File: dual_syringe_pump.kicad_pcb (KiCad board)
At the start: 2 copper layers, 100.3 x 85.5 mm, 163 parts, among them J2 Barrel_Jack_Switch_Pin3Ring, Q1 SS8050, Q2 SS8050, Q3 SS8050, Q4 SS8050, U1 ESP32-WROOM-32, U2 AMS1117-3.3, U3 CH340C, U4 TP5100, U5 LM2596S-buck, U6 TMC2209-LA, U7 TMC2209-LA

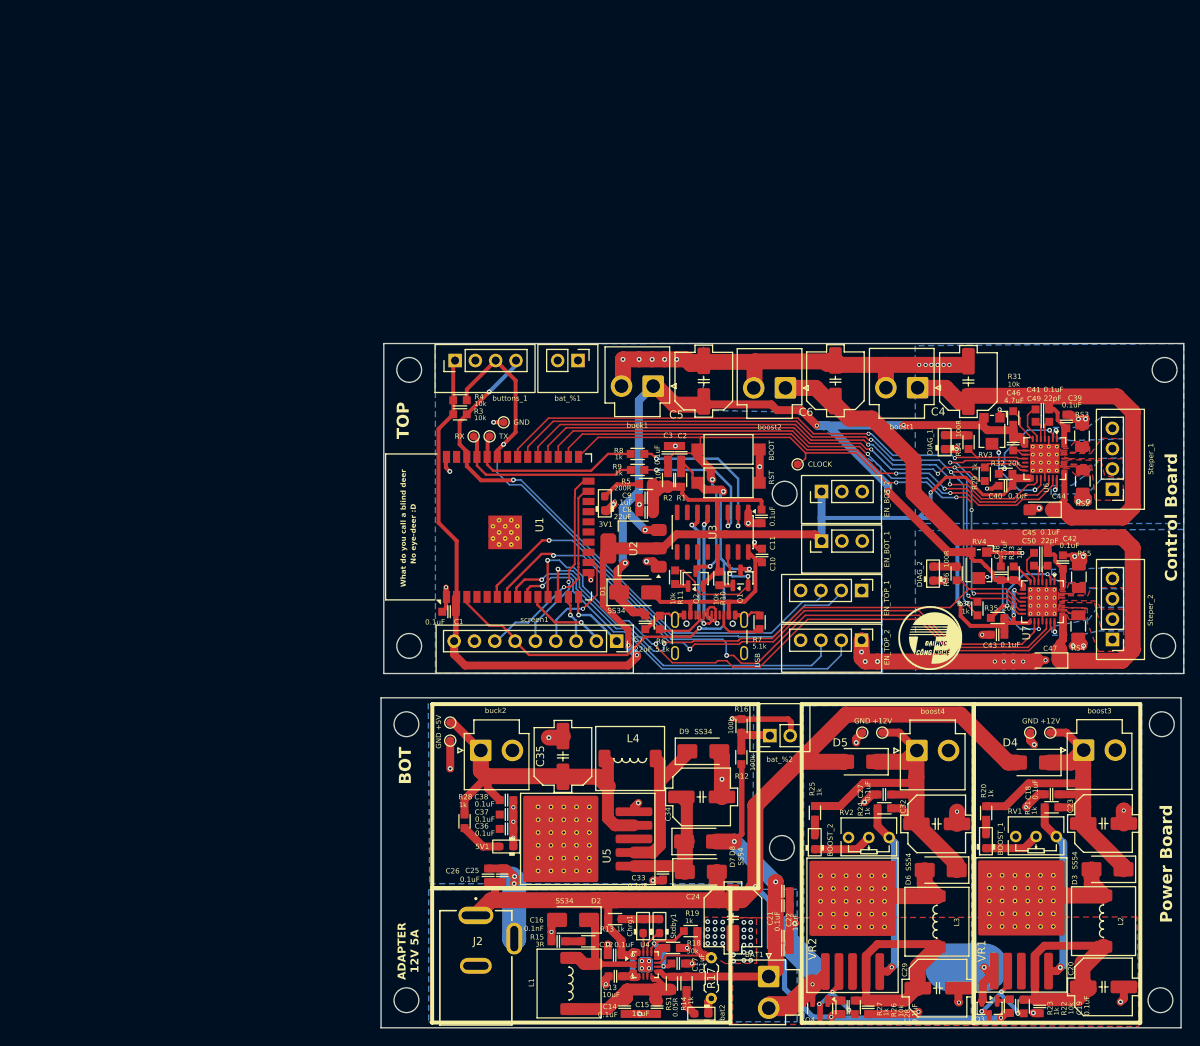
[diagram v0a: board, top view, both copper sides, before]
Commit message: added power button
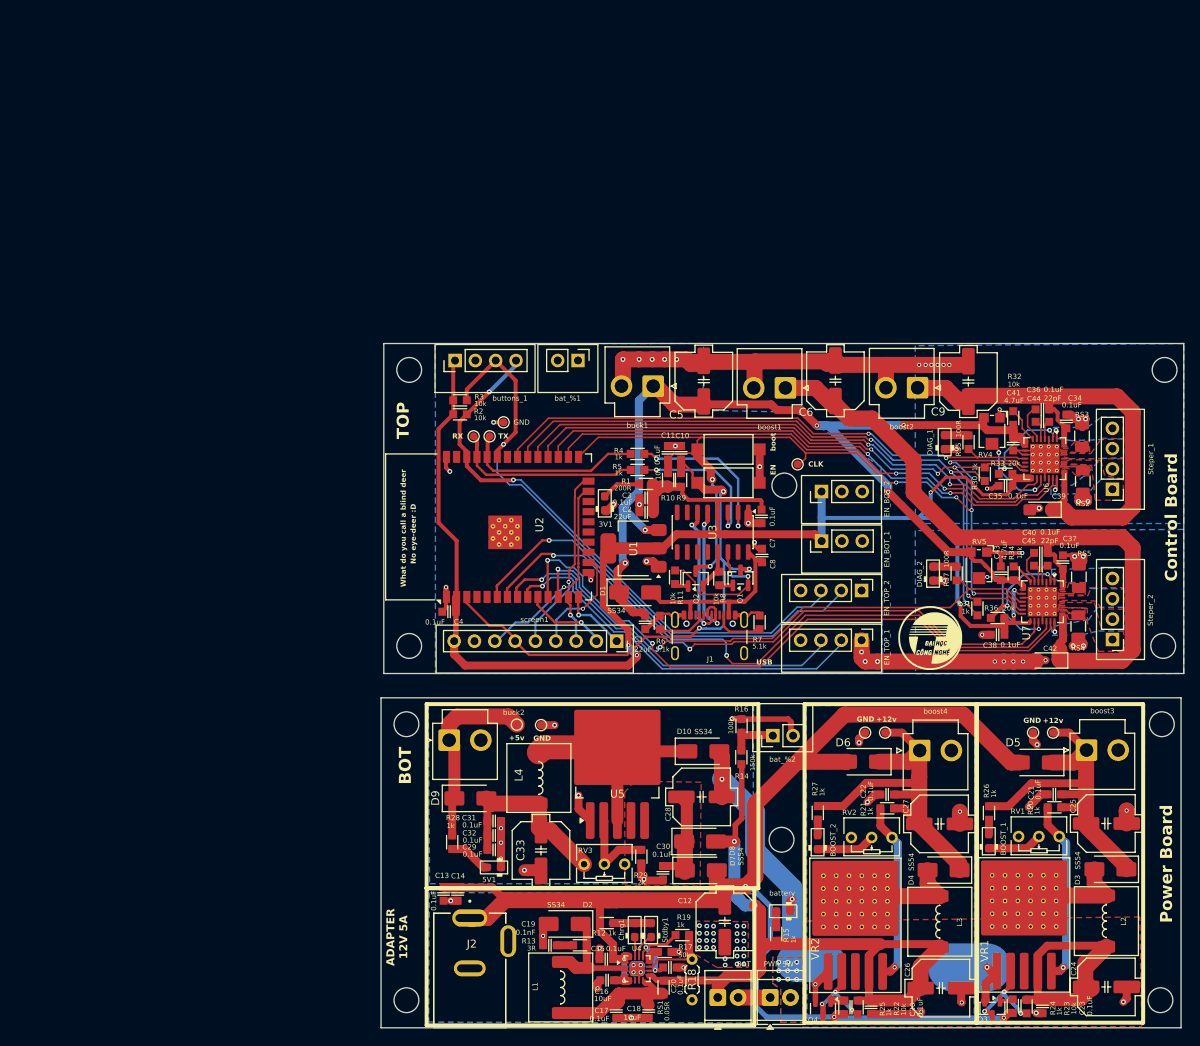
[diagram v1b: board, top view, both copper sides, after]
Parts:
- removed the C21 at (109.8, 93.1)
- removed the C22 at (109.8, 94.8)
- removed the C30 at (109.8, 87.5)
- removed the C31 at (109.8, 89.3)
- added D9: SS34, Diode_SMD:D_SMA, F.Cu at (70.8, 75.9)
- added PWR SW: pb, TerminalBlock_TE-Connectivity:TerminalBlock_TE_282834-2_1x02_P2.54mm_Horizontal, F.Cu at (108.2, 100.8)
- added R29: 2k, PCM_4ms_Resistor:R_0603, F.Cu at (92.1, 83.2)
- added RV3: 10k, PCM_Potentiometer_THT_AKL_Double:Potentiometer_Bourns_3266Y_Vertical, F.Cu at (85.0, 84.1)
- BAT: renamed from BAT1; footprint Connector_JST:JST_VH_B2P-VH-B_1x02_P3.96mm_Vertical -> TerminalBlock_TE-Connectivity:TerminalBlock_TE_282834-2_1x02_P2.54mm_Horizontal
- R14: renamed from R12; value 100k -> 150k
- TP1: renamed from CLOCK; value TestPoint -> clock
- TP2: renamed from RX; value TestPoint -> rx
- TP3: renamed from TX; value TestPoint -> tx
- U5: value LM2596S-buck -> XL4015; footprint PCM_Package_TO_SOT_SMD_AKL:TO-263-5_TabPin3_ThermalVias -> Package_TO_SOT_SMD:TO-263-5_TabPin3
- moved battery 16.4 mm to (109.9, 90.0)
- moved R15 12.8 mm to (109.0, 92.8), turned to -90 degrees
- moved C33 12.1 mm to (79.6, 82.4), turned to -90 degrees
- moved L4 11.7 mm to (79.3, 73.3), turned to -90 degrees
- moved TP7 11.5 mm to (79.6, 66.7), turned to 180 degrees
- moved U5 10.6 mm to (89.1, 71.0), turned to 90 degrees
- moved TP8 8.33 mm to (76.6, 66.7), turned to 180 degrees
- moved C14 7.68 mm to (67.4, 87.8), turned to -90 degrees
- moved BAT 6.88 mm to (101.7, 100.8), turned to 0 degrees
- moved C13 4.48 mm to (69.2, 87.8), turned to -90 degrees
- moved buck2 4.15 mm to (68.1, 68.6)
- moved 5V1 3.04 mm to (73.7, 84.5)
- moved C29 3.04 mm to (73.8, 82.3)
- moved C31 3.04 mm to (73.8, 78.7)
- moved C32 3.04 mm to (73.8, 80.5)
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- renumbered C7 to C1, C2 to C10, C3 to C11, C24 to C12, C25 to C13, C26 to C14, C12 to C15, C13 to C16, C14 to C17, C15 to C18, C16 to C19, C8 to C2, C17 to C20, C18 to C21, C27 to C22, C19 to C23, C20 to C24, C23 to C25, C29 to C26, C32 to C27, C34 to C28, C36 to C29, C9 to C3, C33 to C30, C28 to C30, C38 to C31, C37 to C32, C35 to C33, C39 to C34, C40 to C35, C41 to C36, C42 to C37, C43 to C38, C44 to C39, C1 to C4, C45 to C40, C46 to C41, C47 to C42, C48 to C43, C49 to C44, C50 to C45, C11 to C7, C10 to C8, C4 to C9, D9 to D10, D6 to D4, D4 to D5, D5 to D6, EN_TOP_2 to EN_TOP_1, EN_TOP_1 to EN_TOP_2, USB to J1, R5 to R1, R2 to R10, R13 to R12, R15 to R13, R14 to R15, R18 to R17, R17 to R18, R3 to R2, R21 to R20, R24 to R21, R26 to R22, R22 to R23, R23 to R24, R27 to R25, R20 to R26, R25 to R27, R4 to R3, R29 to R30, R30 to R31, R31 to R32, R32 to R33, R33 to R34, R34 to R35, R35 to R36, R36 to R37, R8 to R4, R9 to R5, R10 to R8, R1 to R9, RV3 to RV4, RV4 to RV5, RST to SW1, BOOT to SW2, +12V to TP4, +12V to TP5, GND to TP6, GND to TP7, +5V to TP8, GND to TP9, U2 to U1, U1 to U2, bat2 to battery, boost2 to boost1, boost1 to boost2
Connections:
- net /BTN1 renamed /bat%
- BAT pad 2: GND -> Earth
- C12 pad 2: GND -> Earth
- C13 pad 2: GND -> Earth
- C14 pad 2: GND -> Earth
- C15 pad 2: GND -> Earth
- C16 pad 2: GND -> Earth
- C17 pad 2: GND -> Earth
- C18 pad 2: GND -> Earth
- C19 pad 2: GND -> Earth
- C20 pad 2: GND -> Earth
- C29 pad 1: +5V -> Net-(D9-A)
- C31 pad 1: +5V -> Net-(D9-A)
- C32 pad 1: +5V -> Net-(D9-A)
- C33 pad 1: +5V -> Net-(D9-A)
- D10 pad 1: Net-(D9-K) -> Net-(D10-K)
- D2 pad 2: GND -> Earth
- J2 pad 2: GND -> Earth
- J2 pad 3: GND -> Earth
- L4 pad 1: Net-(D9-K) -> Net-(D10-K)
- L4 pad 2: +5V -> Net-(D9-A)
- R17 pad 1: GND -> Earth
- R18 pad 1: GND -> Earth
- R22 pad 1: Net-(Q4-C) -> Vbat
- R22 pad 2: Vbat -> Net-(Q4-C)
- R23 pad 1: Net-(Q3-C) -> Vbat
- R23 pad 2: Vbat -> Net-(Q3-C)
- U2 pad 4: /BTN2 -> unconnected-(U2-SENSOR_VP-Pad4)
- U2 pad 5: /BTN3 -> unconnected-(U2-SENSOR_VN-Pad5)
- U4 pad 17: GND -> Earth
- U4 pad 7: GND -> Earth
- U5 pad 1: Net-(D7-K) -> GND
- U5 pad 2: Net-(D9-K) -> /Power Circuits/FB
- U5 pad 3: GND -> Net-(D10-K)
- U5 pad 4: +5V -> Net-(D7-K)
- U5 pad 5: GND -> Net-(D7-K)
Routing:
- net Net-(D10-K): track 0.00 -> 28.9 mm
- net Net-(D9-A): track 0.00 -> 23.9 mm
- net +5V: track 171.3 -> 149.5 mm
- net Earth: track 0.00 -> 20.9 mm, vias 0 -> 37
- net Net-(D9-K): track 19.5 -> 0.00 mm
- net GND: track 136.3 -> 117.9 mm, vias 60 -> 31
- net Vbat: track 107.5 -> 125.7 mm
- net /Power Circuits/FB: track 0.00 -> 10.8 mm
- net Adapter_+12V: track 186.5 -> 180.5 mm
- net /Power Circuits/NTC: track 11.9 -> 9.59 mm
- net Net-(D7-K): track 16.8 -> 15.0 mm
- net Net-(bat2-A): track 3.35 -> 2.00 mm
- net /SDA1: track 48.8 -> 48.1 mm
- net /SCL1: track 47.9 -> 47.2 mm
- net esp32_CLK: track 117.9 -> 117.4 mm
- added copper zone on B.Cu, net Earth
- added copper zone on F.Cu, net Earth
- added copper zone on F.Cu, net Net-(D7-K)
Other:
- outline, holes or cut-outs redrawn
- board text added: "+12v"
- board text added: "+5v"
- board text added: "CLK"
- board text added: "EN"
- board text added: "GND"
- board text added: "RX"
- board text added: "TX"
- board text added: "USB"
- board text added: "boot"

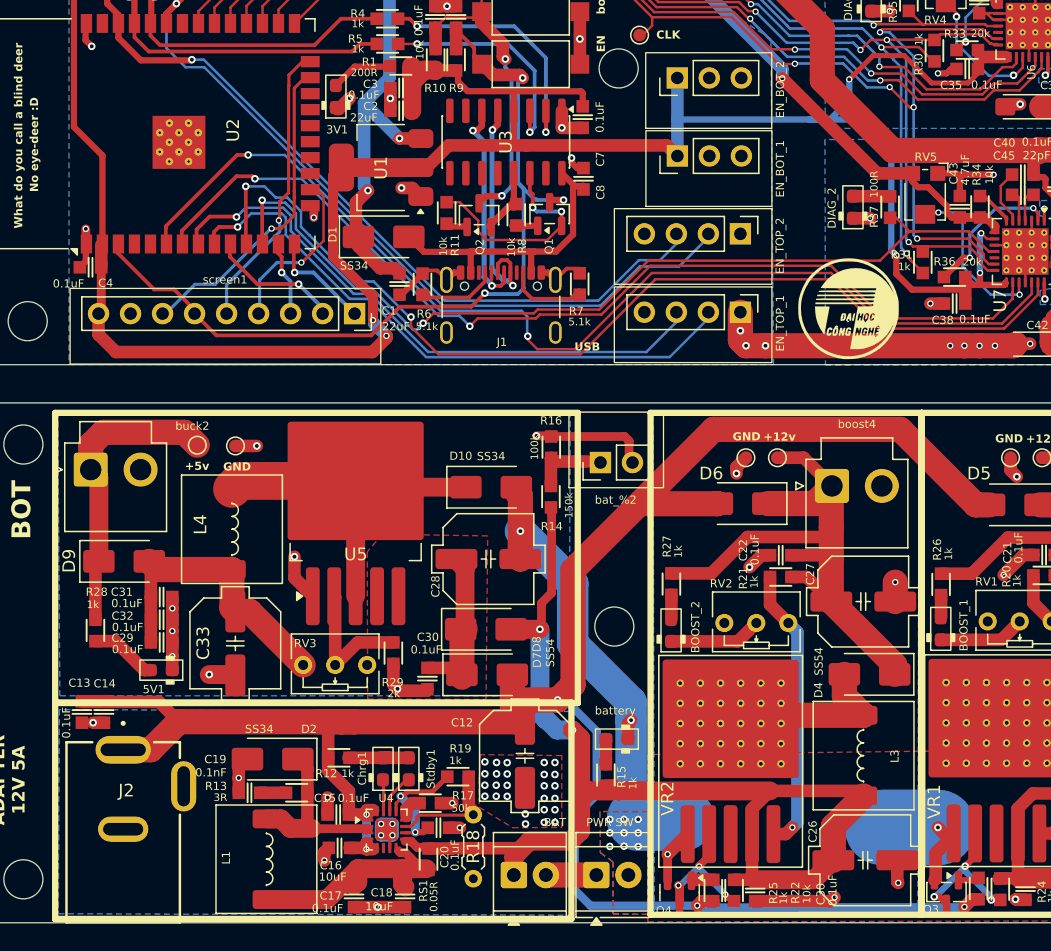
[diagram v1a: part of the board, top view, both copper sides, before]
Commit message: changed star gnd
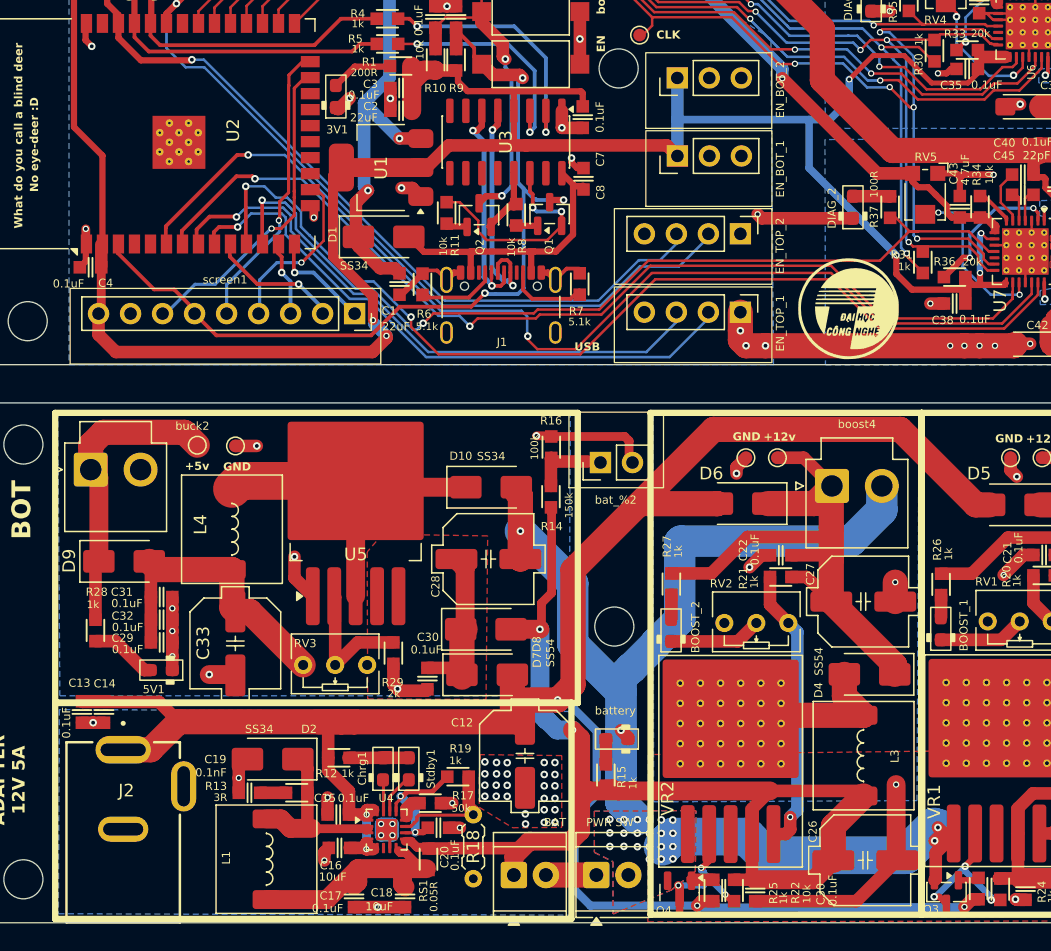
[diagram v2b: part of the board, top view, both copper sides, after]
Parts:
- moved G*** 23.5 mm to (127.5, 83.8)
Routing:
- net GND: track 117.9 -> 179.2 mm, vias 31 -> 42
- net GND1: track 164.3 -> 170.6 mm
- net +3.3V: track 203.7 -> 201.5 mm
- net Net-(Q4-C): track 12.2 -> 13.3 mm
- net Earth: track 20.9 -> 21.8 mm

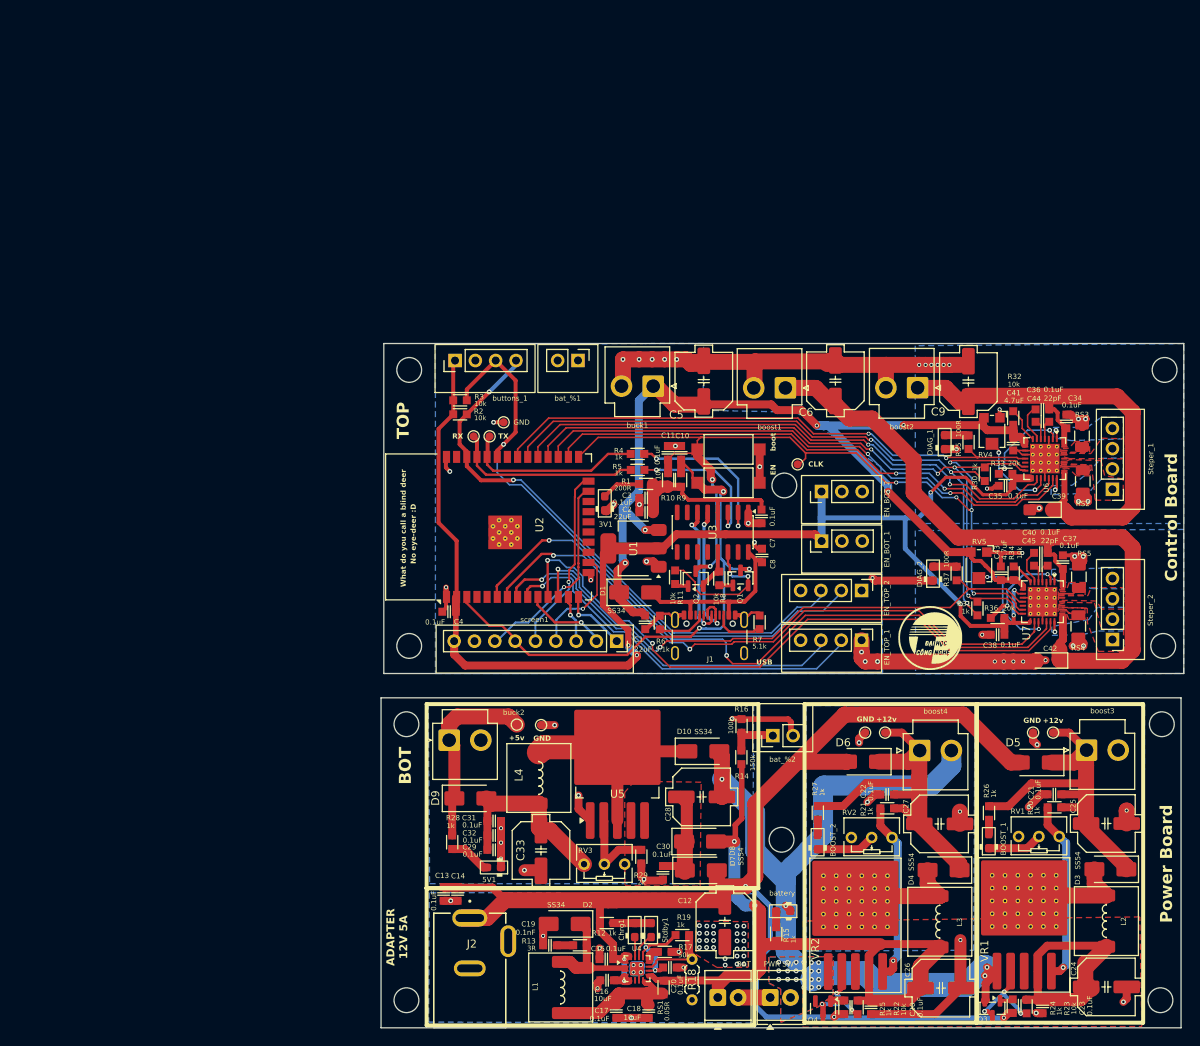
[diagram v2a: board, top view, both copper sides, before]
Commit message: changed silk screen, added grid for star ground
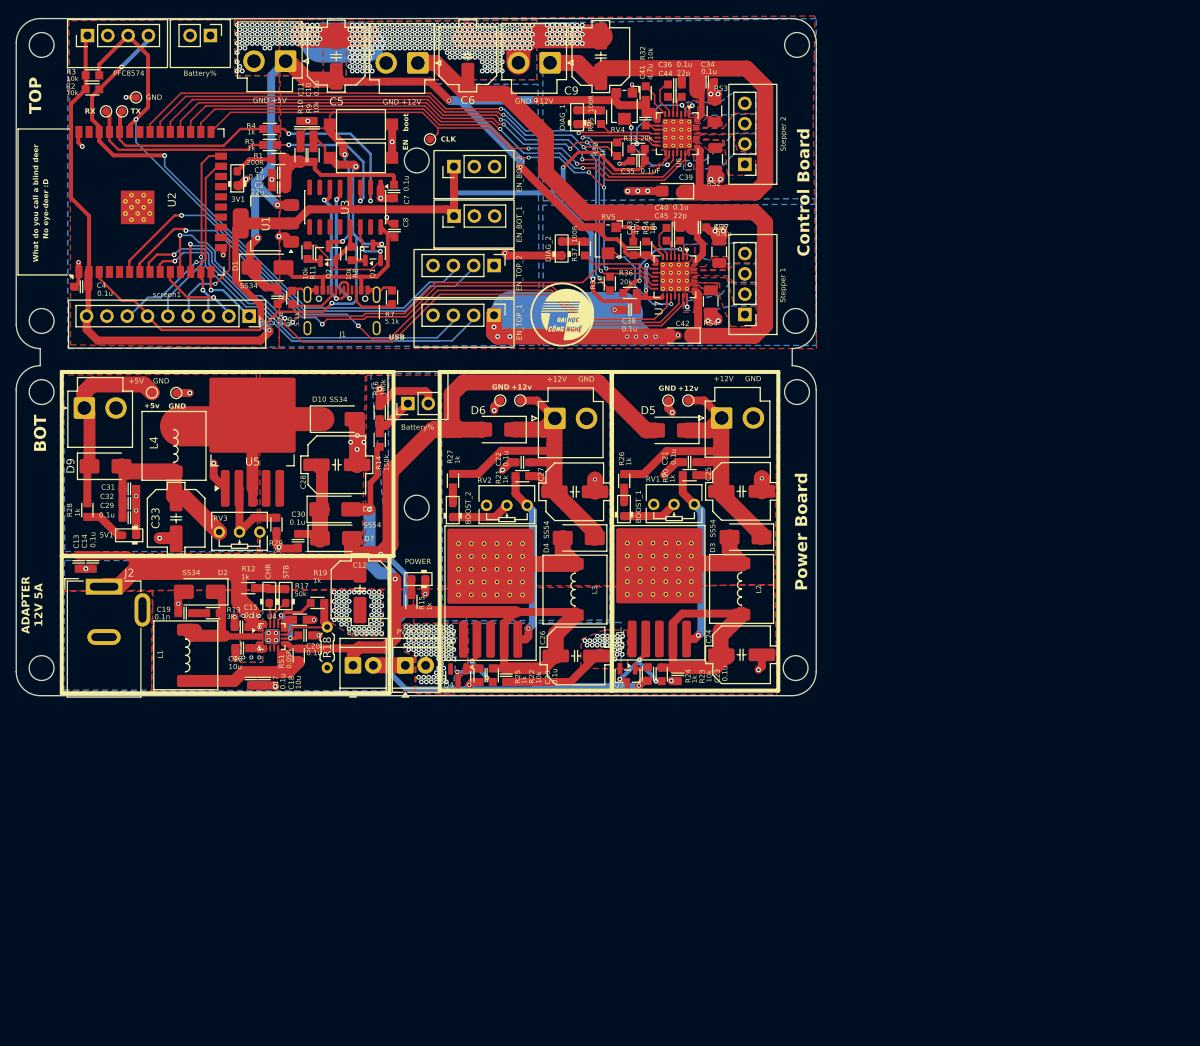
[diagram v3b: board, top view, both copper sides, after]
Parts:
- +12V     GND: renamed from boost4
- +12V     GND: renamed from boost3
- +5V    GND: renamed from buck2
- C1, C2: value 22uF -> 22u
- C10, C13, C15, C17, C20, C21, C22, C23, C3, C30 (x2), C31, C34, C36, C37, C38, C4, C40, C7: value 0.1uF -> 0.1u
- C16, C18: value 10uF -> 10u
- C19: value 0.1nF -> 0.1n
- C41, C43: value 4.7uF -> 4.7u
- C44, C45: value 22pF -> 22p
- GND +12V: renamed from boost1
- GND +12V: renamed from boost2
- GND +5V: renamed from buck1
- J2: footprint my_custom_footprint:GCT_DCJ200-10-A-XX-K_REVA -> Connector_BarrelJack:BarrelJack_GCT_DCJ200-10-A_Horizontal
- PWR SWT: renamed from PWR SW
- Stepper 1: renamed from Steper_2
- Stepper 2: renamed from Steper_1
- moved J2 66.3 mm to (25.0, 49.4)
- moved C18 63.5 mm to (45.0, 60.9)
- moved L1 62.6 mm to (35.2, 58.0)
- moved CHR 61.9 mm to (45.6, 50.6)
- moved STB 61.9 mm to (47.7, 50.6)
- moved R13 61.9 mm to (38.6, 52.7)
- moved C34 61.8 mm to (100.4, -13.6), turned to 0 degrees
- moved C37 61.8 mm to (99.4, 4.53), turned to 0 degrees
- moved C17 61.7 mm to (43.4, 60.9)
- moved R37 61.7 mm to (85.1, 7.18)
- moved DIAG_2 61.7 mm to (82.2, 7.16)
- moved D4 61.7 mm to (84.3, 43.3)
- moved TP4 61.7 mm to (98.0, 26.2)
- moved TP6 61.7 mm to (95.5, 26.2)
- moved +12V     GND 61.7 mm to (81.3, 28.4)
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- renumbered BAT to BATTERY, bat_%2 to Battery%, bat_%1 to Battery%, Chrg1 to CHR, buttons_1 to PFC8574, battery to POWER, Stdby1 to STB
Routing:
- net GND: track 179.2 -> 79.6 mm, vias 42 -> 137
- net GND1: track 170.6 -> 188.2 mm, vias 45 -> 453
- net Adapter_+12V: track 180.5 -> 186.6 mm, vias 5 -> 11
- net Net-(U7-BRB): track 3.76 -> 0.00 mm
- net +12V_2: track 138.0 -> 141.3 mm
- net Net-(U4-VS): track 19.6 -> 22.6 mm
- net +12V_1: track 111.8 -> 114.7 mm
- net +3.3V: track 201.5 -> 204.3 mm
- net Vbat: track 125.7 -> 123.3 mm
- net Net-(D2-K): track 16.2 -> 18.6 mm
- net Net-(U6-BRA): track 2.49 -> 0.34 mm
- net /SDA: track 78.3 -> 76.8 mm
- net Net-(Chrg1-A): track 5.30 -> 3.87 mm
- net Net-(Steper_1-Pin_2): track 1.53 -> 0.11 mm
- net Net-(bat_%2-Pin_1): track 5.28 -> 6.42 mm
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- added copper zone on F.Cu, net (none)
- added copper zone on F.Cu, net +12V_1
- added copper zone on F.Cu, net +12V_2
- added copper zone on F.Cu, net +3.3V
- added copper zone on F.Cu, net +5V
- added copper zone on B.Cu, net Adapter_+12V
- added copper zone on F.Cu, net Adapter_+12V
- added copper zone on F.Cu, net GND1
- added copper zone on F.Cu, net Net-(Steper_1-Pin_2)
- added copper zone on F.Cu, net Net-(Steper_1-Pin_4)
- added copper zone on F.Cu, net Net-(Steper_2-Pin_2)
- added copper zone on F.Cu, net Net-(Steper_2-Pin_4)
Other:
- board size 100.3 x 85.5 mm -> 100 x 84.6 mm
